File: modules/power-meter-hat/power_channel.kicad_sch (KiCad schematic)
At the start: 8 parts, among them J4 Conn_01x02, U4 INA219AxD

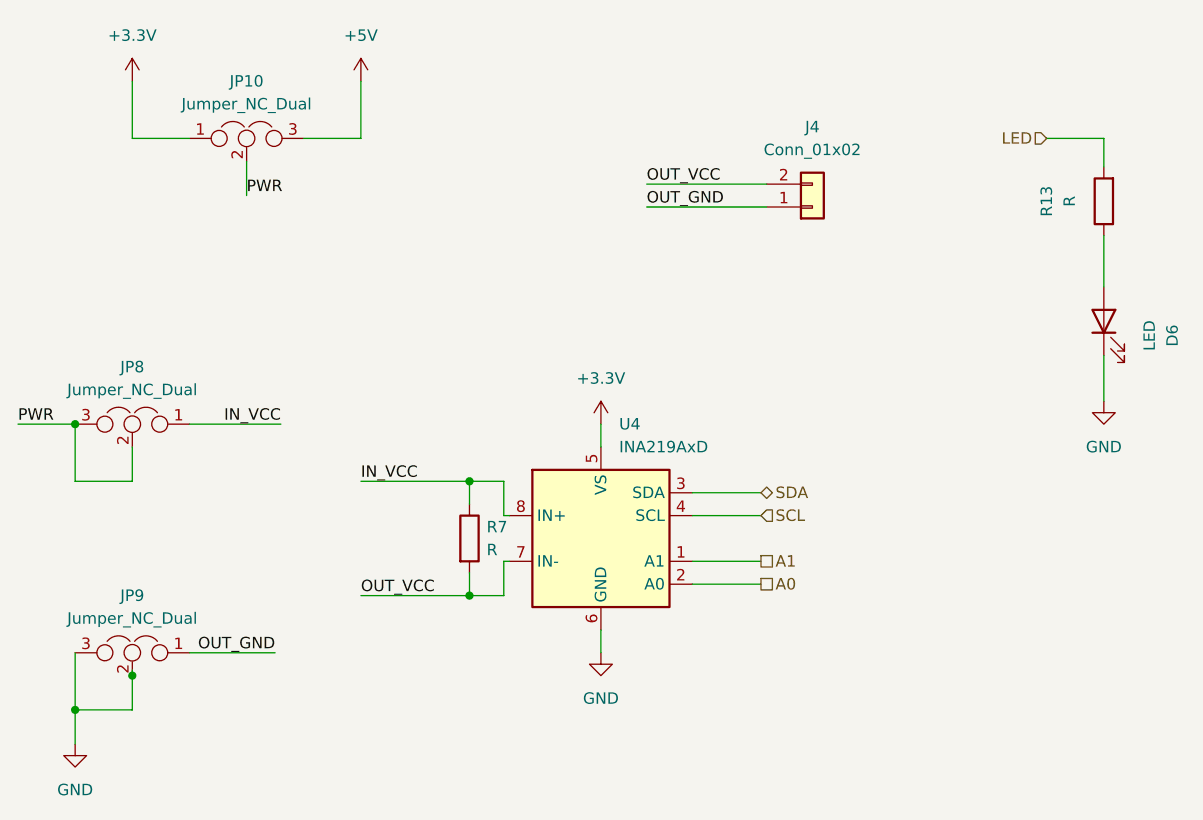
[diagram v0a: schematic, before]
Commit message: Add external power source
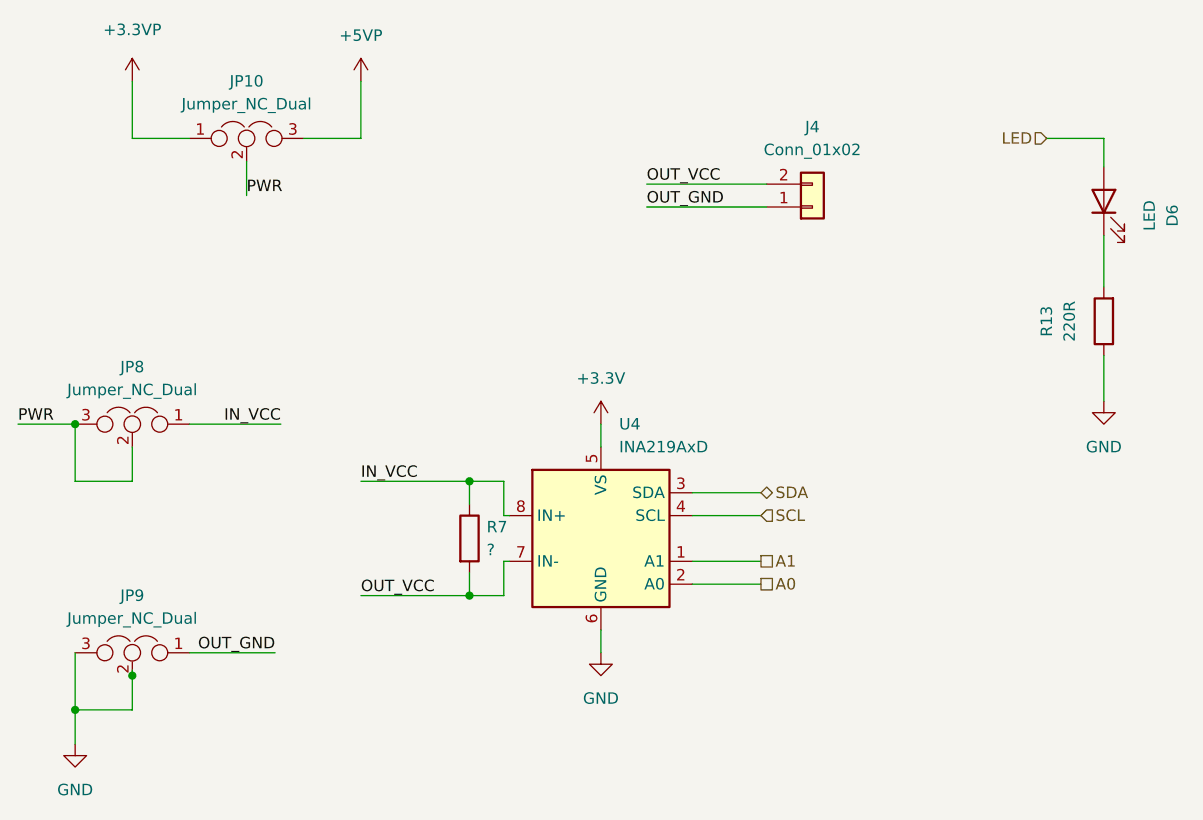
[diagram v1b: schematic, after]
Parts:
- R13: value R -> 220R
- R7: value R -> ?
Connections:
- net +3V3: no longer JP10.1
- net GND: now also R13.1; no longer D6.1 (K)
- net LED: now also D6.2 (A); no longer R13.2
- net +5V renamed +5VP
- new net: D6.1 (K), R13.2
- new net +3.3VP: JP10.1
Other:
- moved on the sheet: D6, R13
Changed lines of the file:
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@@
     (pin "3")
-  )
-  (symbol (lib_id "power:+5V") (at 101.6 25.4 0)
-    (in_bom yes) (on_board yes) (fields_autoplaced)
-    (property "Reference" "#PWR0122" (id 0) (at 101.6 29.21 0)
-      (effects (font (size 1.27 1.27)) hide)
-    )
-    (property "Value" "+5V" (id 1) (at 101.6 20.32 0))
-    (property "Footprint" "" (id 2) (at 101.6 25.4 0)
-      (effects (font (size 1.27 1.27)) hide)
-    )
-    (property "Datasheet" "" (id 3) (at 101.6 25.4 0)
-      (effects (font (size 1.27 1.27)) hide)
-    )
-    (pin "1")
   )
   (symbol (lib_id "power:+3.3V") (at 128.27 63.5 0)
@@
       (effects (font (size 1.27 1.27)) (justify left))
     )
-    (property "Value" "R" (id 1) (at 115.57 77.4699 0)
+    (property "Value" "?" (id 1) (at 115.57 77.4699 0)
       (effects (font (size 1.27 1.27)) (justify left))
     )
@@
     (pin "8")
   )
-  (symbol (lib_id "Device:R") (at 184.15 38.735 180)
+  (symbol (lib_id "Device:R") (at 184.15 52.07 180)
     (in_bom yes) (on_board yes) (fields_autoplaced)
-    (property "Reference" "R13" (id 0) (at 177.8 38.735 90))
-    (property "Value" "R" (id 1) (at 180.34 38.735 90))
-    (property "Footprint" "Resistor_SMD:R_0805_2012Metric_Pad1.20x1.40mm_HandSolder" (id 2) (at 185.928 38.735 90)
+    (property "Reference" "R13" (id 0) (at 177.8 52.07 90))
+    (property "Value" "220R" (id 1) (at 180.34 52.07 90))
+    (property "Footprint" "Resistor_SMD:R_0805_2012Metric_Pad1.20x1.40mm_HandSolder" (id 2) (at 185.928 52.07 90)
       (effects (font (size 1.27 1.27)) hide)
     )
-    (property "Datasheet" "~" (id 3) (at 184.15 38.735 0)
+    (property "Datasheet" "~" (id 3) (at 184.15 52.07 0)
       (effects (font (size 1.27 1.27)) hide)
     )
@@
     (pin "3")
   )
-  (symbol (lib_id "Device:LED") (at 184.15 52.07 90)
+  (symbol (lib_id "power:+3.3VP") (at 76.2 25.4 0)
     (in_bom yes) (on_board yes) (fields_autoplaced)
-    (property "Reference" "D6" (id 0) (at 191.77 53.6575 0))
-    (property "Value" "LED" (id 1) (at 189.23 53.6575 0))
-    (property "Footprint" "LED_SMD:LED_1206_3216Metric_Castellated" (id 2) (at 184.15 52.07 0)
+    (property "Reference" "#PWR0121" (id 0) (at 80.01 26.67 0)
       (effects (font (size 1.27 1.27)) hide)
     )
-    (property "Datasheet" "~" (id 3) (at 184.15 52.07 0)
+    (property "Value" "+3.3VP" (id 1) (at 76.2 19.685 0))
+    (property "Footprint" "" (id 2) (at 76.2 25.4 0)
+      (effects (font (size 1.27 1.27)) hide)
+    )
+    (property "Datasheet" "" (id 3) (at 76.2 25.4 0)
+      (effects (font (size 1.27 1.27)) hide)
+    )
+    (pin "1")
+  )
+  (symbol (lib_id "Device:LED") (at 184.15 38.735 90)
+    (in_bom yes) (on_board yes) (fields_autoplaced)
+    (property "Reference" "D6" (id 0) (at 191.77 40.3225 0))
+    (property "Value" "LED" (id 1) (at 189.23 40.3225 0))
+    (property "Footprint" "LED_SMD:LED_1206_3216Metric_Castellated" (id 2) (at 184.15 38.735 0)
+      (effects (font (size 1.27 1.27)) hide)
+    )
+    (property "Datasheet" "~" (id 3) (at 184.15 38.735 0)
       (effects (font (size 1.27 1.27)) hide)
     )
     (pin "1")
     (pin "2")
+  )
+  (symbol (lib_id "power:+5VP") (at 101.6 25.4 0)
+    (in_bom yes) (on_board yes) (fields_autoplaced)
+    (property "Reference" "#PWR0122" (id 0) (at 101.6 29.21 0)
+      (effects (font (size 1.27 1.27)) hide)
+    )
+    (property "Value" "+5VP" (id 1) (at 101.6 20.32 0))
+    (property "Footprint" "" (id 2) (at 101.6 25.4 0)
+      (effects (font (size 1.27 1.27)) hide)
+    )
+    (property "Datasheet" "" (id 3) (at 101.6 25.4 0)
+      (effects (font (size 1.27 1.27)) hide)
+    )
+    (pin "1")
   )
   (symbol (lib_id "power:GND") (at 128.27 88.9 0)
@@
       (effects (font (size 1.27 1.27)) hide)
     )
-    (pin "1")
-  )
-  (symbol (lib_id "power:+3.3V") (at 76.2 25.4 0)
-    (in_bom yes) (on_board yes) (fields_autoplaced)
-    (property "Reference" "#PWR0121" (id 0) (at 76.2 29.21 0)
-      (effects (font (size 1.27 1.27)) hide)
-    )
-    (property "Value" "+3.3V" (id 1) (at 76.2 20.32 0))
-    (property "Footprint" "" (id 2) (at 76.2 25.4 0)
-      (effects (font (size 1.27 1.27)) hide)
-    )
-    (property "Datasheet" "" (id 3) (at 76.2 25.4 0)
-      (effects (font (size 1.27 1.27)) hide)
-    )

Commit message: Replace pin sockets with screw terminals
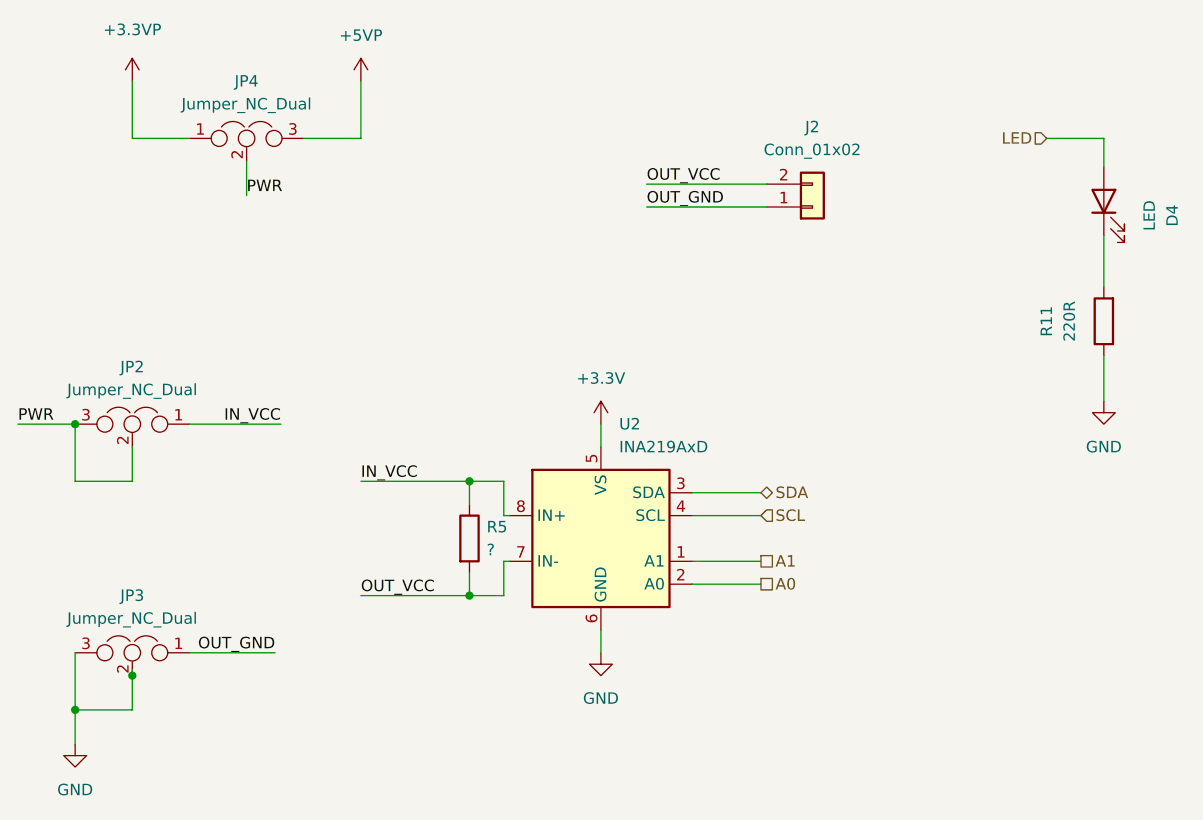
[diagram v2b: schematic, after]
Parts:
- J2: renamed from J4; footprint Connector_PinSocket_2.54mm:PinSocket_1x02_P2.54mm_Vertical -> TerminalBlock_Phoenix:TerminalBlock_Phoenix_PT-1,5-2-3.5-H_1x02_P3.50mm_Horizontal
- renumbered D6 to D4, JP8 to JP2, JP9 to JP3, JP10 to JP4, R13 to R11, R7 to R5, U4 to U2
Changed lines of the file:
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@@
   (symbol (lib_id "Device:Jumper_NC_Dual") (at 76.2 63.5 0) (mirror y)
     (in_bom yes) (on_board yes) (fields_autoplaced)
-    (property "Reference" "JP8" (id 0) (at 76.2 57.15 0))
+    (property "Reference" "JP2" (id 0) (at 76.2 57.15 0))
     (property "Value" "Jumper_NC_Dual" (id 1) (at 76.2 59.69 0))
     (property "Footprint" "Connector_PinHeader_2.54mm:PinHeader_1x03_P2.54mm_Vertical" (id 2) (at 76.2 63.5 0)
@@
   (symbol (lib_id "power:+3.3V") (at 128.27 63.5 0)
     (in_bom yes) (on_board yes) (fields_autoplaced)
-    (property "Reference" "#PWR0119" (id 0) (at 128.27 67.31 0)
+    (property "Reference" "#PWR0109" (id 0) (at 128.27 67.31 0)
       (effects (font (size 1.27 1.27)) hide)
     )
@@
   (symbol (lib_id "Device:R") (at 113.665 76.2 0)
     (in_bom yes) (on_board yes) (fields_autoplaced)
-    (property "Reference" "R7" (id 0) (at 115.57 74.9299 0)
+    (property "Reference" "R5" (id 0) (at 115.57 74.9299 0)
       (effects (font (size 1.27 1.27)) (justify left))
     )
@@
   (symbol (lib_id "Analog_ADC:INA219AxD") (at 128.27 76.2 0)
     (in_bom yes) (on_board yes) (fields_autoplaced)
-    (property "Reference" "U4" (id 0) (at 130.2894 63.5 0)
+    (property "Reference" "U2" (id 0) (at 130.2894 63.5 0)
       (effects (font (size 1.27 1.27)) (justify left))
     )
@@
   (symbol (lib_id "Device:R") (at 184.15 52.07 180)
     (in_bom yes) (on_board yes) (fields_autoplaced)
-    (property "Reference" "R13" (id 0) (at 177.8 52.07 90))
+    (property "Reference" "R11" (id 0) (at 177.8 52.07 90))
     (property "Value" "220R" (id 1) (at 180.34 52.07 90))
     (property "Footprint" "Resistor_SMD:R_0805_2012Metric_Pad1.20x1.40mm_HandSolder" (id 2) (at 185.928 52.07 90)
@@
   (symbol (lib_id "power:GND") (at 69.85 99.06 0)
     (in_bom yes) (on_board yes) (fields_autoplaced)
-    (property "Reference" "#PWR0123" (id 0) (at 69.85 105.41 0)
+    (property "Reference" "#PWR0113" (id 0) (at 69.85 105.41 0)
       (effects (font (size 1.27 1.27)) hide)
     )
@@
   (symbol (lib_id "Connector_Generic:Conn_01x02") (at 151.765 39.37 0) (mirror x)
     (in_bom yes) (on_board yes) (fields_autoplaced)
-    (property "Reference" "J4" (id 0) (at 151.765 30.48 0))
+    (property "Reference" "J2" (id 0) (at 151.765 30.48 0))
     (property "Value" "Conn_01x02" (id 1) (at 151.765 33.02 0))
-    (property "Footprint" "Connector_PinSocket_2.54mm:PinSocket_1x02_P2.54mm_Vertical" (id 2) (at 151.765 39.37 0)
+    (property "Footprint" "TerminalBlock_Phoenix:TerminalBlock_Phoenix_PT-1,5-2-3.5-H_1x02_P3.50mm_Horizontal" (id 2) (at 151.765 39.37 0)
       (effects (font (size 1.27 1.27)) hide)
     )
@@
   (symbol (lib_id "power:GND") (at 184.15 60.96 0)
     (in_bom yes) (on_board yes) (fields_autoplaced)
-    (property "Reference" "#PWR0131" (id 0) (at 184.15 67.31 0)
+    (property "Reference" "#PWR0129" (id 0) (at 184.15 67.31 0)
       (effects (font (size 1.27 1.27)) hide)
     )
@@
   (symbol (lib_id "Device:Jumper_NC_Dual") (at 88.9 31.75 0)
     (in_bom yes) (on_board yes) (fields_autoplaced)
-    (property "Reference" "JP10" (id 0) (at 88.9 25.4 0))
+    (property "Reference" "JP4" (id 0) (at 88.9 25.4 0))
     (property "Value" "Jumper_NC_Dual" (id 1) (at 88.9 27.94 0))
     (property "Footprint" "Connector_PinHeader_2.54mm:PinHeader_1x03_P2.54mm_Vertical" (id 2) (at 88.9 31.75 0)
@@
   (symbol (lib_id "Device:Jumper_NC_Dual") (at 76.2 88.9 0) (mirror y)
     (in_bom yes) (on_board yes) (fields_autoplaced)
-    (property "Reference" "JP9" (id 0) (at 76.2 82.55 0))
+    (property "Reference" "JP3" (id 0) (at 76.2 82.55 0))
     (property "Value" "Jumper_NC_Dual" (id 1) (at 76.2 85.09 0))
     (property "Footprint" "Connector_PinHeader_2.54mm:PinHeader_1x03_P2.54mm_Vertical" (id 2) (at 76.2 88.9 0)
@@
   (symbol (lib_id "power:+3.3VP") (at 76.2 25.4 0)
     (in_bom yes) (on_board yes) (fields_autoplaced)
-    (property "Reference" "#PWR0121" (id 0) (at 80.01 26.67 0)
+    (property "Reference" "#PWR0111" (id 0) (at 80.01 26.67 0)
       (effects (font (size 1.27 1.27)) hide)
     )
@@
   (symbol (lib_id "Device:LED") (at 184.15 38.735 90)
     (in_bom yes) (on_board yes) (fields_autoplaced)
-    (property "Reference" "D6" (id 0) (at 191.77 40.3225 0))
+    (property "Reference" "D4" (id 0) (at 191.77 40.3225 0))
     (property "Value" "LED" (id 1) (at 189.23 40.3225 0))
     (property "Footprint" "LED_SMD:LED_1206_3216Metric_Castellated" (id 2) (at 184.15 38.735 0)
@@
   (symbol (lib_id "power:+5VP") (at 101.6 25.4 0)
     (in_bom yes) (on_board yes) (fields_autoplaced)
-    (property "Reference" "#PWR0122" (id 0) (at 101.6 29.21 0)
+    (property "Reference" "#PWR0112" (id 0) (at 101.6 29.21 0)
       (effects (font (size 1.27 1.27)) hide)
     )
@@
   (symbol (lib_id "power:GND") (at 128.27 88.9 0)
     (in_bom yes) (on_board yes) (fields_autoplaced)
-    (property "Reference" "#PWR0120" (id 0) (at 128.27 95.25 0)
+    (property "Reference" "#PWR0110" (id 0) (at 128.27 95.25 0)
       (effects (font (size 1.27 1.27)) hide)
     )
